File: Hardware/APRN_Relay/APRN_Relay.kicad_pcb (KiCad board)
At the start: 2 copper layers, 64 x 56 mm, 43 parts, among them J101 SERVO1, J102 SERVO2, J103 PTT, J104 Pi_Zero, J105 RADIO, J106 CHG, J107 PWR, J108 BAT, U101 DHT11, U102 INA219AIDR, U103 NCV1117ST50T3G

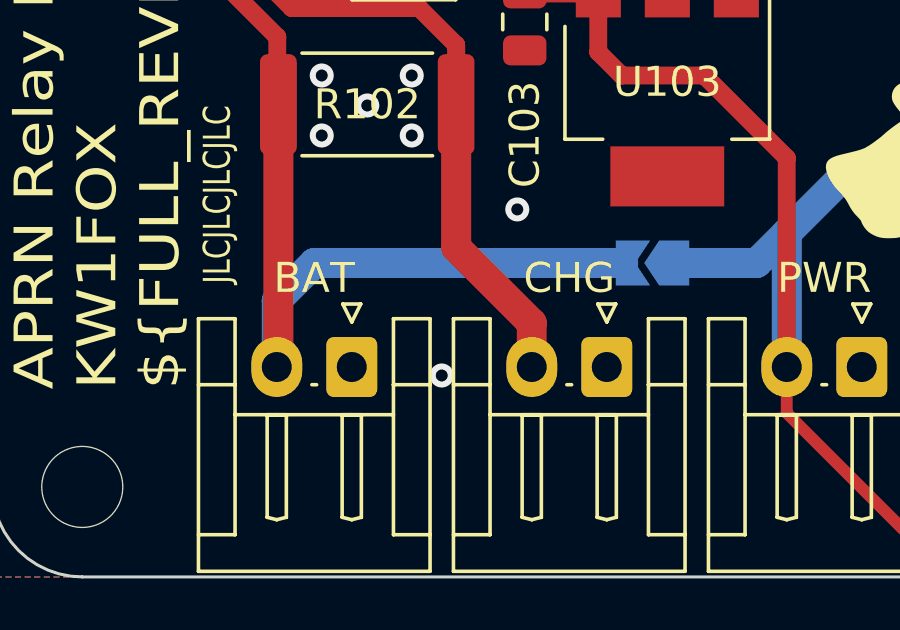
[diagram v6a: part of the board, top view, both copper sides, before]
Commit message: Remove power flag from input of current sensor
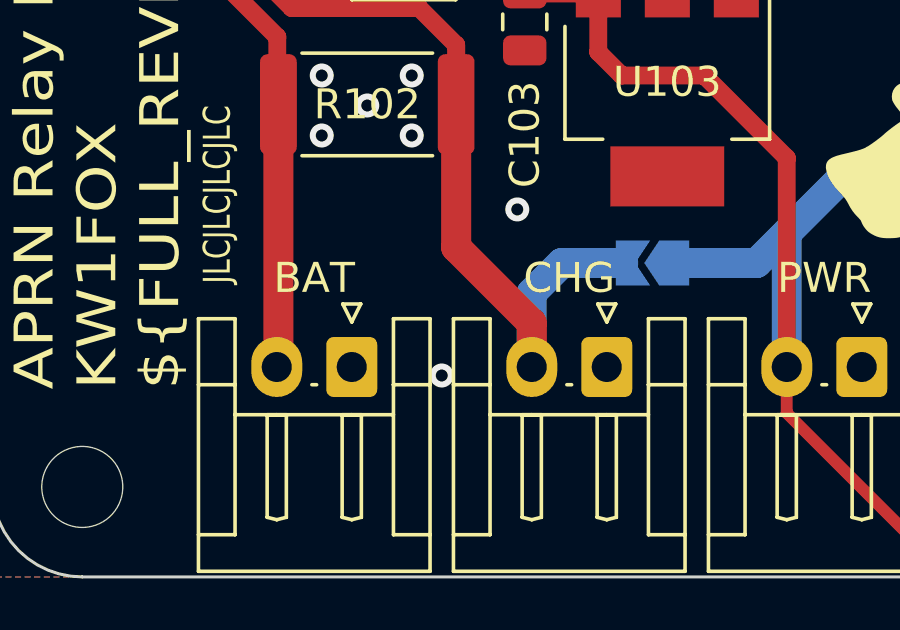
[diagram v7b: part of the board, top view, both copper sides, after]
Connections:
- JP101 pad 2: /BATTERY -> /CHARGE
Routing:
- net /BATTERY: track 36.2 -> 21.9 mm
- net /CHARGE: track 26.0 -> 31.9 mm
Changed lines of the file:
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@@
   (net 42 "/CHARGE")
   (net 43 "/BATTERY")
-  (net 44 "Net-(R111-Pad2)")
+  (net 44 "Net-(D105-Pad1)")
   (footprint "Resistor_SMD:R_0805_2012Metric" (layer "F.Cu")
     (at 164.25 123.75 180)
@@
     (fp_circle (center 1.27 0) (end 2.77 0) (layer "F.Fab") (width 0.1) (fill none))
     (pad "1" thru_hole rect (at 0 0 270) (size 1.8 1.8) (drill 0.9) (layers *.Cu *.Mask)
-      (net 44 "Net-(R111-Pad2)") (pinfunction "K") (pintype "passive"))
+      (net 44 "Net-(D105-Pad1)") (pinfunction "K") (pintype "passive"))
     (pad "2" thru_hole circle (at 2.54 0 270) (size 1.8 1.8) (drill 0.9) (layers *.Cu *.Mask)
       (net 35 "/POWER") (pinfunction "A") (pintype "passive"))
@@
       (net 28 "GND") (pintype "passive"))
     (pad "2" smd roundrect (at 0.9125 0 180) (size 1.025 1.4) (layers "F.Cu" "F.Paste" "F.Mask") (roundrect_rratio 0.243902)
-      (net 44 "Net-(R111-Pad2)") (pintype "passive"))
+      (net 44 "Net-(D105-Pad1)") (pintype "passive"))
     (model "${KICAD6_3DMODEL_DIR}/Resistor_SMD.3dshapes/R_0805_2012Metric.wrl"
       (offset (xyz 0 0 0))
@@
       ))
     (pad "2" smd custom (at 0.725 0 180) (size 0.3 0.3) (layers "B.Cu" "B.Mask")
-      (net 43 "/BATTERY") (pinfunction "B") (pintype "passive") (zone_connect 2)
+      (net 42 "/CHARGE") (pinfunction "B") (pintype "passive") (zone_connect 2)
       (options (clearance outline) (anchor rect))
       (primitives
@@
   (segment (start 131.25 123) (end 128.73 120.48) (width 1) (layer "F.Cu") (net 42))
   (segment (start 122.05 106.432056) (end 122.3625 106.119556) (width 0.6) (layer "F.Cu") (net 42))
+  (segment (start 131.25 122) (end 132.25 121) (width 1) (layer "B.Cu") (net 42))
+  (segment (start 132.25 121) (end 134.3 121) (width 1) (layer "B.Cu") (net 42))
+  (segment (start 131.25 124.4675) (end 131.25 122) (width 1) (layer "B.Cu") (net 42))
   (segment (start 121.25 111.947056) (end 122.7675 113.464556) (width 0.6) (layer "F.Cu") (net 43))
   (segment (start 122.400444 104.849556) (end 121.25 106) (width 0.6) (layer "F.Cu") (net 43))
@@
   (segment (start 122.7675 115.677056) (end 122.805 115.714556) (width 0.6) (layer "F.Cu") (net 43))
   (segment (start 121.25 106) (end 121.25 111.947056) (width 0.6) (layer "F.Cu") (net 43))
-  (segment (start 122.75 124.4675) (end 122.75 122.25) (width 1) (layer "B.Cu") (net 43))
-  (segment (start 124 121) (end 134.3 121) (width 1) (layer "B.Cu") (net 43))
-  (segment (start 122.75 122.25) (end 124 121) (width 1) (layer "B.Cu") (net 43))
   (segment (start 148.3375 123.75) (end 148.3375 127.369556) (width 0.4) (layer "F.Cu") (net 44))
   (segment (start 148.3375 127.369556) (end 148.2675 127.439556) (width 0.4) (layer "F.Cu") (net 44))

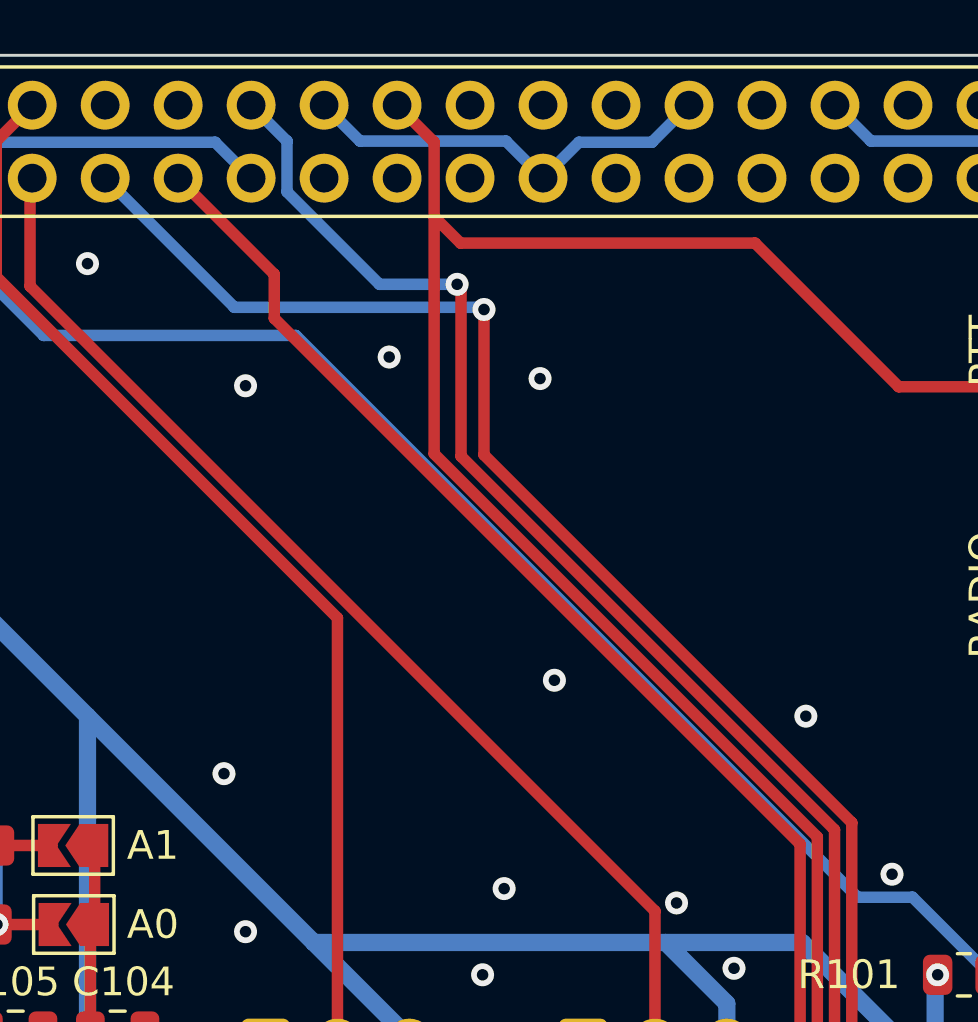
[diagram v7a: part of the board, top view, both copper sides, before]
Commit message: Add kicad logo to back
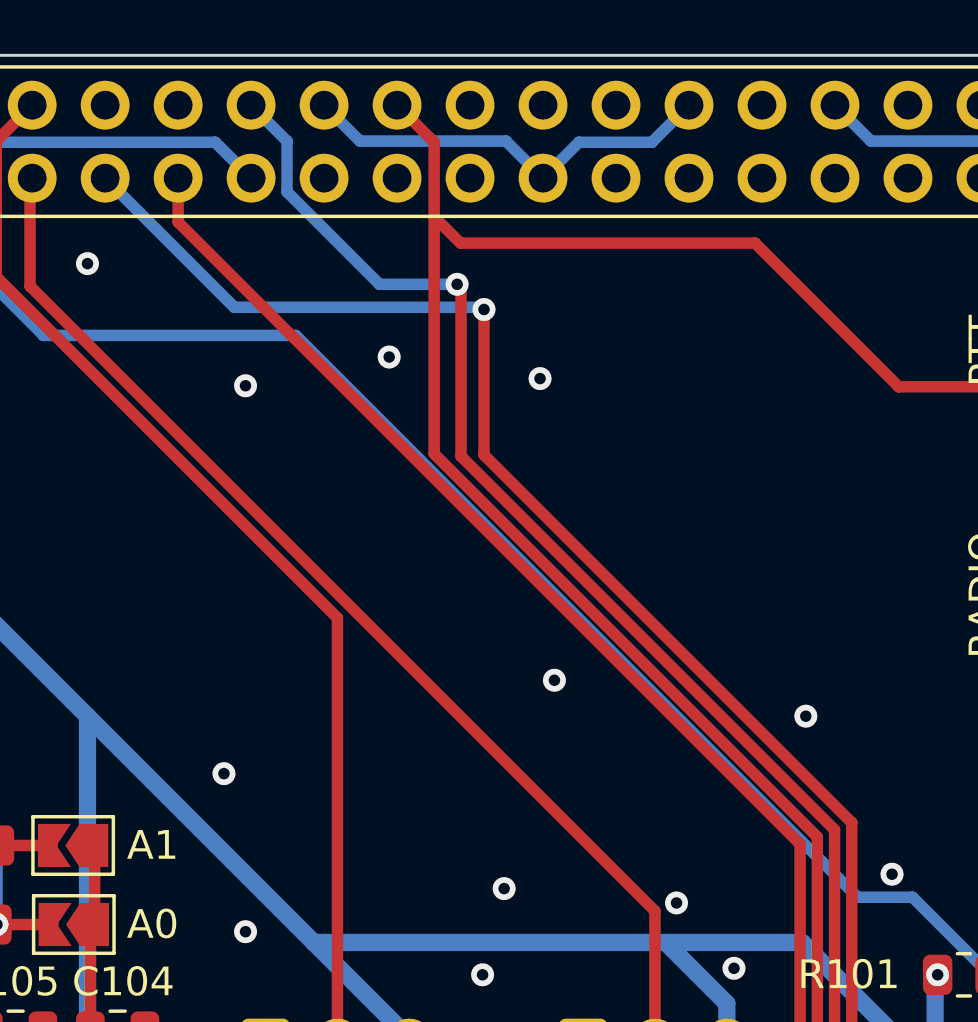
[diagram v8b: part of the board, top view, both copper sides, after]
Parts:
- added REF**: KiCad-Logo_6mm_SilkScreen, Symbol:KiCad-Logo_6mm_SilkScreen, B.Cu at (168.8, 122.2)
